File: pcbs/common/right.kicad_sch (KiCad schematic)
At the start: 89 parts, among them J2 TRS

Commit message: first pass at the gecko
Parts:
- removed rEXLED? (x2): YS-SK6812MINI-E, kbd_local:YS-SK6812MINI-E, symbol kbd_local:YS-SK6812MINI-E
- removed rEXSW? (x2): RotaryEncoder_Switch, kbd_local:keyswitch_cherrymx_hotswap_1u_rotary_encoder_ec12, symbol Device:RotaryEncoder_Switch
- added rEXLED1, rEXLED2: YS-SK6812MINI-E, kbd_local:YS-SK6812MINI-E, symbol kbd_local:YS-SK6812MINI-E
- added rRE1, rRE2: RotaryEncoder, kbd:rotary_encoder_EC05E_Vert, symbol Device:RotaryEncoder
- added rRE1-2, rRE1-3, rRE2-2, rRE2-3: RotaryEncoder, kbd:rotary_encoder_EC05E, symbol Device:RotaryEncoder
- added rSW22, rSW23: SW_Push, kbd:keyswitch_cherrymx_hotswap_1u, symbol Switch:SW_Push
- rSW? (x4): footprint kbd:keyswitch_cherrymx_hotswap_1u -> kbd:keyswitch_choc12_hotswap_1u
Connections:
- net GNDR: now also rEXLED1.3 (VSS), rEXLED2.3 (VSS), rRE1-2.C, rRE1-3.C, rRE1.C, rRE2-2.C, rRE2-3.C, rRE2.C, rSW22.2, rSW23.2
- net RE0A: now also rRE1-2.A, rRE1-3.A, rRE1.A
- net RE1A: now also rRE2-2.A, rRE2-3.A, rRE2.A
- net REB: now also rRE1-2.B, rRE1-3.B, rRE1.B, rRE2-2.B, rRE2-3.B, rRE2.B
- net at rD?.1 (K), rLED?.1 (VDD), rLED?.1 (VDD)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: now also rEXLED1.1 (VDD), rEXLED2.1 (VDD)
- net at rLED?.4 (DIN): now also rEXLED1.2 (DOUT); no longer rLED?.2 (DOUT)
- net KEYEX1 renamed KEY22
- net KEY22: now also rSW22.1
- net KEYEX2 renamed KEY23
- net KEY23: now also rSW23.1
- new net: rEXLED1.4 (DIN), rEXLED2.2 (DOUT)
- new net: rEXLED2.4 (DIN), rLED?.2 (DOUT)

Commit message: moved subsheets across
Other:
- company: foostan -> Dane Evans
- title: Corne Right -> Gecko Right
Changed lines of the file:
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@@
 	(paper "A3")
 	(title_block
-		(title "Corne Right")
+		(title "Gecko Right")
 		(date "2023-10-07")
-		(rev "4.0.0")
-		(company "foostan")
+		(rev "1.0.0")
+		(company "Dane Evans")
+		(comment 1 "original: foostan's crkbd 4.1")
 	)
 	(junction
@@
 		)
 		(instances
-			(project "corne-chocolate"
+			(project "Gecko_choc"
 				(path "/4cc5d416-57f5-4147-8183-e03ae6b1198a/50d96a5e-3d25-4129-9495-15388c76587f"
 					(reference "#PWR085")
@@
 		)
 		(instances
-			(project "corne-chocolate"
+			(project "Gecko_choc"
 				(path "/4cc5d416-57f5-4147-8183-e03ae6b1198a/50d96a5e-3d25-4129-9495-15388c76587f"
 					(reference "#PWR087")
@@
 				)
 			)
-			(project "corne-cherry"
+			(project "Gecko_choc"
 				(path "/4cc5d416-57f5-4147-8183-e03ae6b1198a/50d96a5e-3d25-4129-9495-15388c76587f"
 					(reference "#PWR070")
@@
 				)
 			)
-			(project "corne-cherry"
+			(project "Gecko_choc"
 				(path "/4cc5d416-57f5-4147-8183-e03ae6b1198a/50d96a5e-3d25-4129-9495-15388c76587f"
 					(reference "#PWR065")
@@
 				)
 			)
-			(project "corne-cherry"
+			(project "Gecko_choc"
 				(path "/4cc5d416-57f5-4147-8183-e03ae6b1198a/50d96a5e-3d25-4129-9495-15388c76587f"
 					(reference "#PWR069")
@@
 				)
 			)
-			(project "corne-cherry"
+			(project "Gecko_choc"
 				(path "/4cc5d416-57f5-4147-8183-e03ae6b1198a/50d96a5e-3d25-4129-9495-15388c76587f"
 					(reference "rBT4")
@@
 		)
 		(instances
-			(project "corne-chocolate"
+			(project "Gecko_choc"
 				(path "/4cc5d416-57f5-4147-8183-e03ae6b1198a/50d96a5e-3d25-4129-9495-15388c76587f"
 					(reference "rEXLED1")
@@
 				)
 			)
-			(project "corne-cherry"
+			(project "Gecko_choc"
 				(path "/4cc5d416-57f5-4147-8183-e03ae6b1198a/50d96a5e-3d25-4129-9495-15388c76587f"
 					(reference "#PWR066")
@@
 		)
 		(instances
-			(project "corne-chocolate"
+			(project "Gecko_choc"
 				(path "/4cc5d416-57f5-4147-8183-e03ae6b1198a/50d96a5e-3d25-4129-9495-15388c76587f"
 					(reference "rRE2")
@@
 		)
 		(instances
-			(project "corne-chocolate"
+			(project "Gecko_choc"
 				(path "/4cc5d416-57f5-4147-8183-e03ae6b1198a/50d96a5e-3d25-4129-9495-15388c76587f"
 					(reference "rRE1")
@@
 		)
 		(instances
-			(project "corne-chocolate"
+			(project "Gecko_choc"
 				(path "/4cc5d416-57f5-4147-8183-e03ae6b1198a/50d96a5e-3d25-4129-9495-15388c76587f"
 					(reference "#PWR059")
@@
 		)
 		(instances
-			(project "corne-chocolate"
+			(project "Gecko_choc"
 				(path "/4cc5d416-57f5-4147-8183-e03ae6b1198a/50d96a5e-3d25-4129-9495-15388c76587f"
 					(reference "rRE1-2")
@@
 				)
 			)
-			(project "corne-cherry"
+			(project "Gecko_choc"
 				(path "/4cc5d416-57f5-4147-8183-e03ae6b1198a/50d96a5e-3d25-4129-9495-15388c76587f"
 					(reference "#PWR073")
@@
 				)
 			)
-			(project "corne-cherry"
+			(project "Gecko_choc"
 				(path "/4cc5d416-57f5-4147-8183-e03ae6b1198a/50d96a5e-3d25-4129-9495-15388c76587f"
 					(reference "#PWR068")
@@
 		)
 		(instances
-			(project "corne-chocolate"
+			(project "Gecko_choc"
 				(path "/4cc5d416-57f5-4147-8183-e03ae6b1198a/50d96a5e-3d25-4129-9495-15388c76587f"
 					(reference "rSW22")
@@
 		)
 		(instances
-			(project "corne-chocolate"
+			(project "Gecko_choc"
 				(path "/4cc5d416-57f5-4147-8183-e03ae6b1198a/50d96a5e-3d25-4129-9495-15388c76587f"
 					(reference "rRE2-3")
@@
 		)
 		(instances
-			(project "corne-chocolate"
+			(project "Gecko_choc"
 				(path "/4cc5d416-57f5-4147-8183-e03ae6b1198a/50d96a5e-3d25-4129-9495-15388c76587f"
 					(reference "rRE2-2")
@@
 				)
 			)
-			(project "corne-cherry"
+			(project "Gecko_choc"
 				(path "/4cc5d416-57f5-4147-8183-e03ae6b1198a/50d96a5e-3d25-4129-9495-15388c76587f"
 					(reference "#PWR07")
@@
 		)
 		(instances
-			(project "corne-chocolate"
+			(project "Gecko_choc"
 				(path "/4cc5d416-57f5-4147-8183-e03ae6b1198a/50d96a5e-3d25-4129-9495-15388c76587f"
 					(reference "#PWR084")
@@
 				)
 			)
-			(project "corne-cherry"
+			(project "Gecko_choc"
 				(path "/4cc5d416-57f5-4147-8183-e03ae6b1198a/50d96a5e-3d25-4129-9495-15388c76587f"
 					(reference "#PWR075")
@@
 		)
 		(instances
-			(project "corne-chocolate"
+			(project "Gecko_choc"
 				(path "/4cc5d416-57f5-4147-8183-e03ae6b1198a/50d96a5e-3d25-4129-9495-15388c76587f"
 					(reference "#PWR086")
@@
 				)
 			)
-			(project "corne-cherry"
+			(project "Gecko_choc"
 				(path "/4cc5d416-57f5-4147-8183-e03ae6b1198a/50d96a5e-3d25-4129-9495-15388c76587f"
 					(reference "#PWR072")
@@
 		)
 		(instances
-			(project "corne-chocolate"
+			(project "Gecko_choc"
 				(path "/4cc5d416-57f5-4147-8183-e03ae6b1198a/50d96a5e-3d25-4129-9495-15388c76587f"
 					(reference "rEXLED2")
@@
 				)
 			)
-			(project "corne-cherry"
+			(project "Gecko_choc"
 				(path "/4cc5d416-57f5-4147-8183-e03ae6b1198a/50d96a5e-3d25-4129-9495-15388c76587f"
 					(reference "#PWR067")
@@
 				)
 			)
-			(project "corne-cherry"
+			(project "Gecko_choc"
 				(path "/4cc5d416-57f5-4147-8183-e03ae6b1198a/50d96a5e-3d25-4129-9495-15388c76587f"
 					(reference "#PWR071")
@@
 		)
 		(instances
-			(project "corne-chocolate"
+			(project "Gecko_choc"
 				(path "/4cc5d416-57f5-4147-8183-e03ae6b1198a/50d96a5e-3d25-4129-9495-15388c76587f"
 					(reference "#PWR074")
@@
 		)
 		(instances
-			(project "corne-chocolate"
+			(project "Gecko_choc"
 				(path "/4cc5d416-57f5-4147-8183-e03ae6b1198a/50d96a5e-3d25-4129-9495-15388c76587f"
 					(reference "rRE1-3")
@@
 				)
 			)
-			(project "corne-cherry"
+			(project "Gecko_choc"
 				(path "/4cc5d416-57f5-4147-8183-e03ae6b1198a/50d96a5e-3d25-4129-9495-15388c76587f"
 					(reference "rBT3")
@@
 		)
 		(instances
-			(project "corne-chocolate"
+			(project "Gecko_choc"
 				(path "/4cc5d416-57f5-4147-8183-e03ae6b1198a/50d96a5e-3d25-4129-9495-15388c76587f"
 					(reference "rSW23")
@@
 				)
 			)
-			(project "corne-cherry"
+			(project "Gecko_choc"
 				(path "/4cc5d416-57f5-4147-8183-e03ae6b1198a/50d96a5e-3d25-4129-9495-15388c76587f"
 					(reference "rJP1")
@@
 				)
 			)
-			(project "corne-cherry"
+			(project "Gecko_choc"
 				(path "/4cc5d416-57f5-4147-8183-e03ae6b1198a/50d96a5e-3d25-4129-9495-15388c76587f"
 					(reference "rBT1")
@@
 				)
 			)
-			(project "corne-cherry"
+			(project "Gecko_choc"
 				(path "/4cc5d416-57f5-4147-8183-e03ae6b1198a/50d96a5e-3d25-4129-9495-15388c76587f"
 					(reference "#PWR076")
@@
 				)
 			)
-			(project "corne-cherry"
+			(project "Gecko_choc"
 				(path "/4cc5d416-57f5-4147-8183-e03ae6b1198a/50d96a5e-3d25-4129-9495-15388c76587f"
 					(reference "rBT2")

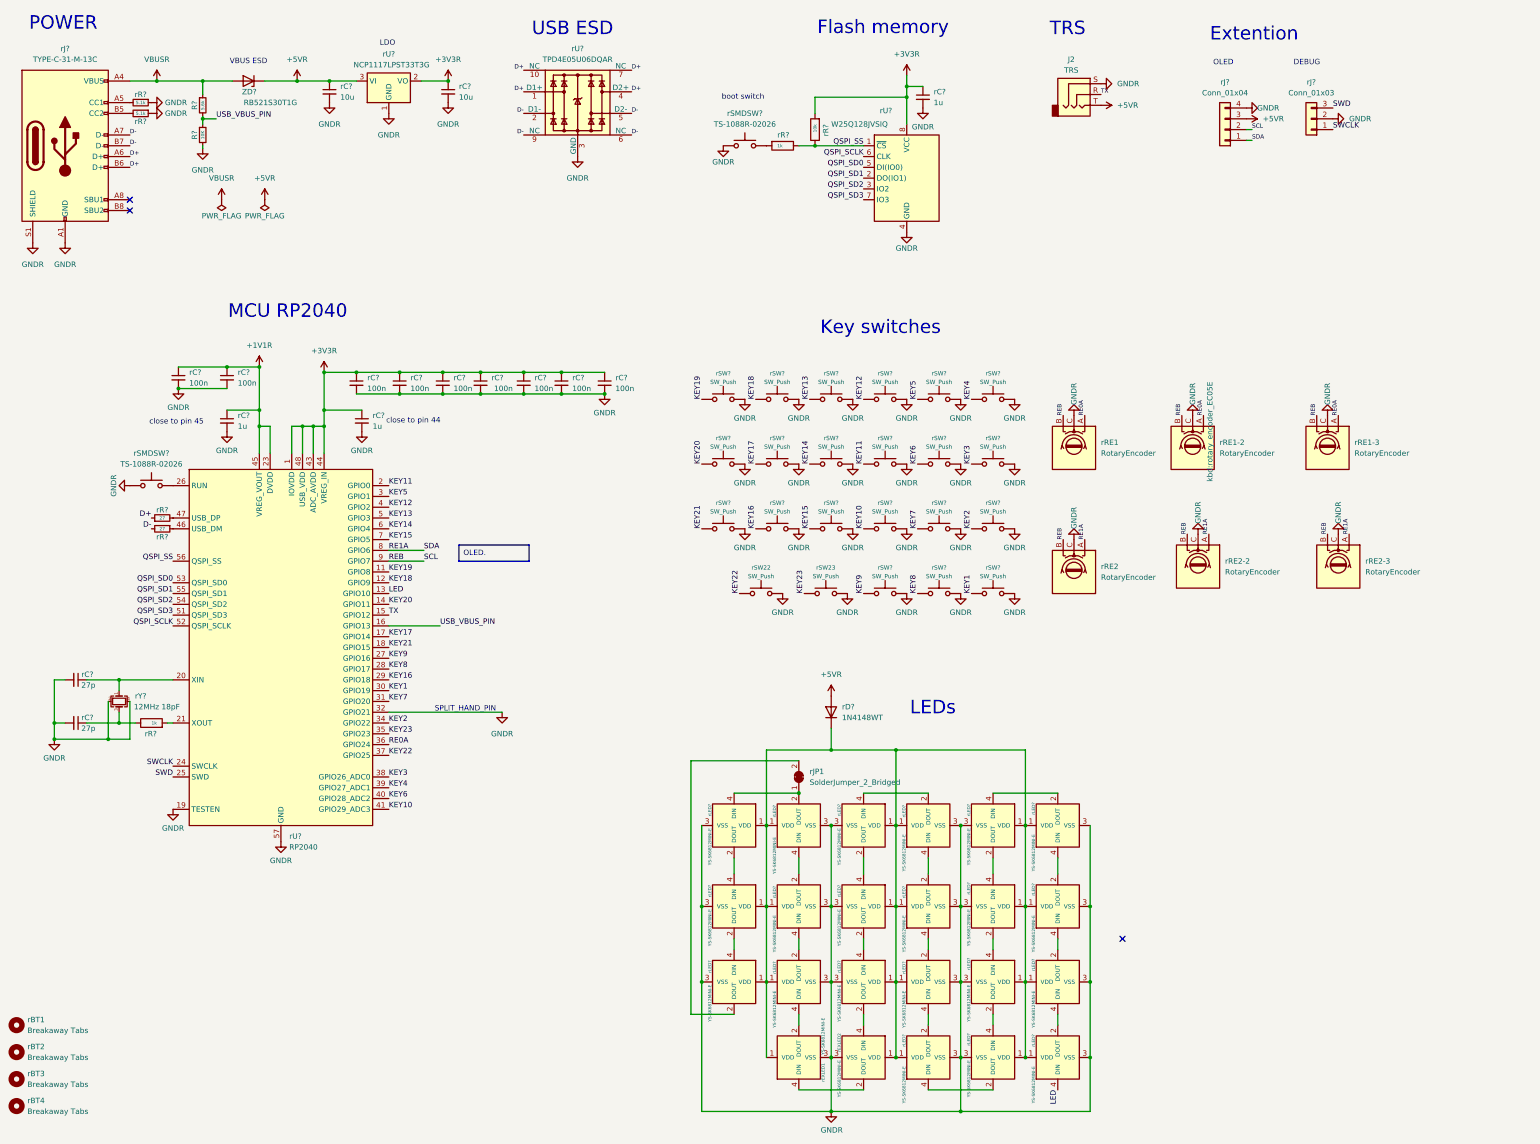
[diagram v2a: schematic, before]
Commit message: add jumpers to the split pin
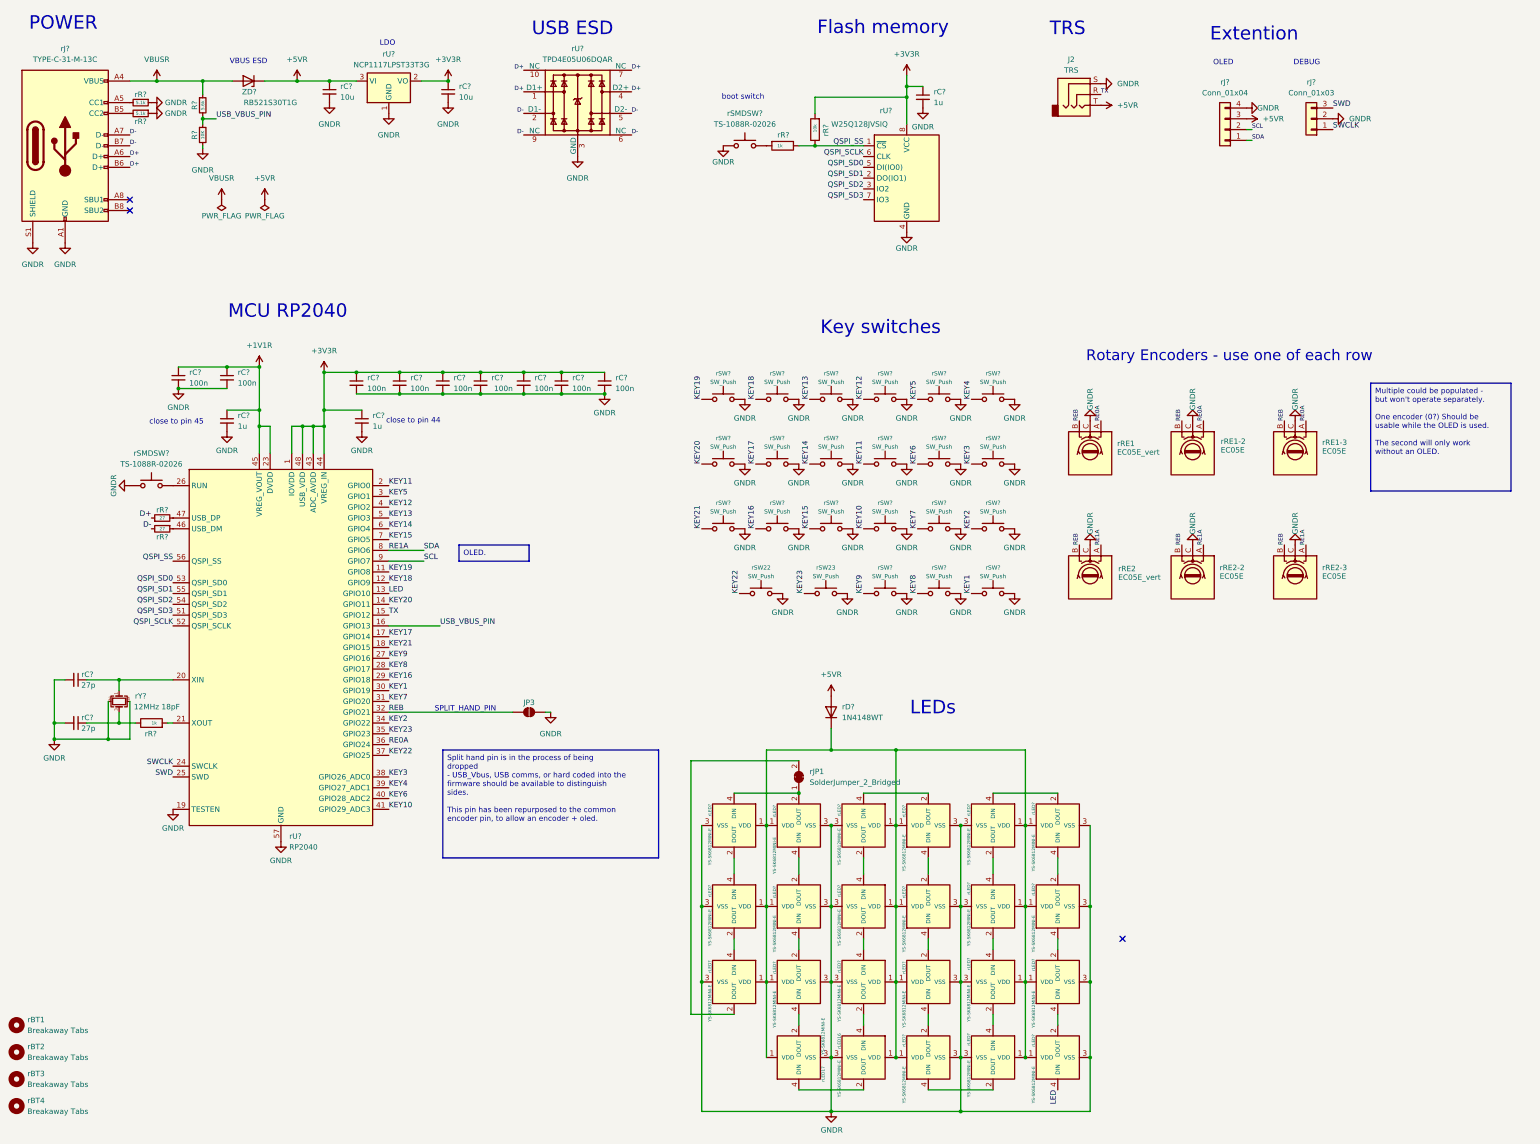
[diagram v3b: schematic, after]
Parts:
- added JP3: SolderJumper_2_Open, Jumper:SolderJumper-2_P1.3mm_Open_RoundedPad1.0x1.5mm, symbol Jumper:SolderJumper_2_Open
- rLED16: renamed from rEXLED2; footprint kbd_local:YS-SK6812MINI-E -> kbd:YS-SK6812MINI-E
- rLED17: renamed from rEXLED1; footprint kbd_local:YS-SK6812MINI-E -> kbd:YS-SK6812MINI-E
- rLED? (x21): footprint kbd_local:YS-SK6812MINI-E -> kbd:YS-SK6812MINI-E
- rRE1, rRE2: value RotaryEncoder -> EC05E_vert
- rRE1-2, rRE1-3, rRE2-2, rRE2-3: value RotaryEncoder -> EC05E
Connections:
- net GNDR: now also JP3.2 (B); no longer rU?.32 (GPIO21)
- net REB: now also rU?.32 (GPIO21), JP3.1 (A); no longer rJ?.2 (Pin_2), rU?.9 (GPIO7)
- new net SCL: rJ?.2 (Pin_2), rU?.9 (GPIO7)
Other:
- note added: "Rotary Encoders - use one of each row"
- moved on the sheet: rRE1, rRE1-2, rRE1-3, rRE2, rRE2-2, rRE2-3

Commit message: allDRC
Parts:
- J2: footprint kbd_local:PJ-398A-5A_PJ-399B-6A -> kbd:PJ-398A-5A_PJ-399B-6A
- rBT1, rBT2, rBT3, rBT4: footprint kbd_local:Breakaway_Tabs -> kbd:Breakaway_Tabs
- rJ?: footprint kbd_local:TYPE-C-31-M-13C -> kbd:TYPE-C-31-M-13C
- rJ?: footprint kbd_local:OLED -> kbd:OLED
- rSMDSW? (x2): footprint kbd_local:TS-1088R-02026 -> kbd:TS-1088R-02026
- rSW22, rSW23, rSW? (x16): footprint kbd:keyswitch_cherrymx_hotswap_1u -> kbd:keyswitch_choc12_hotswap_1u
- rSW?: footprint kbd:keyswitch_cherrymx_hotswap_1.5u -> kbd:keyswitch_choc12_hotswap_1.5u
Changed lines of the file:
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@@
 			)
 		)
-		(property "Footprint" "kbd:keyswitch_cherrymx_hotswap_1u"
+		(property "Footprint" "kbd:keyswitch_choc12_hotswap_1u"
 			(at 236.22 118.11 0)
 			(effects
@@
 			)
 		)
-		(property "Footprint" "kbd:keyswitch_cherrymx_hotswap_1u"
+		(property "Footprint" "kbd:keyswitch_choc12_hotswap_1u"
 			(at 248.92 102.87 0)
 			(effects
@@
 			)
 		)
-		(property "Footprint" "kbd_local:TYPE-C-31-M-13C"
+		(property "Footprint" "kbd:TYPE-C-31-M-13C"
 			(at 34.29 48.26 0)
 			(effects
@@
 			)
 		)
-		(property "Footprint" "kbd:keyswitch_cherrymx_hotswap_1u"
+		(property "Footprint" "kbd:keyswitch_choc12_hotswap_1u"
 			(at 236.22 102.87 0)
 			(effects
@@
 			)
 		)
-		(property "Footprint" "kbd:keyswitch_cherrymx_hotswap_1u"
+		(property "Footprint" "kbd:keyswitch_choc12_hotswap_1u"
 			(at 198.12 133.35 0)
 			(effects
@@
 			)
 		)
-		(property "Footprint" "kbd:keyswitch_cherrymx_hotswap_1u"
+		(property "Footprint" "kbd:keyswitch_choc12_hotswap_1u"
 			(at 210.82 133.35 0)
 			(effects
@@
 			)
 		)
-		(property "Footprint" "kbd:keyswitch_cherrymx_hotswap_1.5u"
+		(property "Footprint" "kbd:keyswitch_choc12_hotswap_1.5u"
 			(at 248.92 148.59 0)
 			(effects
@@
 			)
 		)
-		(property "Footprint" "kbd_local:Breakaway_Tabs"
+		(property "Footprint" "kbd:Breakaway_Tabs"
 			(at 19.05 274.32 0)
 			(effects
@@
 			)
 		)
-		(property "Footprint" "kbd:keyswitch_cherrymx_hotswap_1u"
+		(property "Footprint" "kbd:keyswitch_choc12_hotswap_1u"
 			(at 198.12 118.11 0)
 			(effects
@@
 			)
 		)
-		(property "Footprint" "kbd:keyswitch_cherrymx_hotswap_1u"
+		(property "Footprint" "kbd:keyswitch_choc12_hotswap_1u"
 			(at 185.42 133.35 0)
 			(effects
@@
 			)
 		)
-		(property "Footprint" "kbd:keyswitch_cherrymx_hotswap_1u"
+		(property "Footprint" "kbd:keyswitch_choc12_hotswap_1u"
 			(at 194.31 148.59 0)
 			(effects
@@
 			)
 		)
-		(property "Footprint" "kbd:keyswitch_cherrymx_hotswap_1u"
+		(property "Footprint" "kbd:keyswitch_choc12_hotswap_1u"
 			(at 223.52 148.59 0)
 			(effects
@@
 			)
 		)
-		(property "Footprint" "kbd_local:PJ-398A-5A_PJ-399B-6A"
+		(property "Footprint" "kbd:PJ-398A-5A_PJ-399B-6A"
 			(at 269.24 36.195 0)
 			(effects
@@
 			)
 		)
-		(property "Footprint" "kbd:keyswitch_cherrymx_hotswap_1u"
+		(property "Footprint" "kbd:keyswitch_choc12_hotswap_1u"
 			(at 248.92 133.35 0)
 			(effects
@@
 			)
 		)
-		(property "Footprint" "kbd:keyswitch_cherrymx_hotswap_1u"
+		(property "Footprint" "kbd:keyswitch_choc12_hotswap_1u"
 			(at 236.22 133.35 0)
 			(effects
@@
 			)
 		)
-		(property "Footprint" "kbd_local:TS-1088R-02026"
+		(property "Footprint" "kbd:TS-1088R-02026"
 			(at 50.8 123.19 0)
 			(effects
@@
 			)
 		)
-		(property "Footprint" "kbd:keyswitch_cherrymx_hotswap_1u"
+		(property "Footprint" "kbd:keyswitch_choc12_hotswap_1u"
 			(at 210.82 118.11 0)
 			(effects
@@
 			)
 		)
-		(property "Footprint" "kbd:keyswitch_cherrymx_hotswap_1u"
+		(property "Footprint" "kbd:keyswitch_choc12_hotswap_1u"
 			(at 248.92 118.11 0)
 			(effects
@@
 			)
 		)
-		(property "Footprint" "kbd:keyswitch_cherrymx_hotswap_1u"
+		(property "Footprint" "kbd:keyswitch_choc12_hotswap_1u"
 			(at 185.42 118.11 0)
 			(effects
@@
 			)
 		)
-		(property "Footprint" "kbd_local:OLED"
+		(property "Footprint" "kbd:OLED"
 			(at 303.53 44.45 0)
 			(effects
@@
 			)
 		)
-		(property "Footprint" "kbd:keyswitch_cherrymx_hotswap_1u"
+		(property "Footprint" "kbd:keyswitch_choc12_hotswap_1u"
 			(at 223.52 118.11 0)
 			(effects
@@
 			)
 		)
-		(property "Footprint" "kbd_local:TS-1088R-02026"
+		(property "Footprint" "kbd:TS-1088R-02026"
 			(at 190.5 43.18 0)
 			(effects
@@
 			)
 		)
-		(property "Footprint" "kbd_local:Breakaway_Tabs"
+		(property "Footprint" "kbd:Breakaway_Tabs"
 			(at 19.05 267.97 0)
 			(effects
@@
 			)
 		)
-		(property "Footprint" "kbd:keyswitch_cherrymx_hotswap_1u"
+		(property "Footprint" "kbd:keyswitch_choc12_hotswap_1u"
 			(at 236.22 148.59 0)
 			(effects
@@
 			)
 		)
-		(property "Footprint" "kbd:keyswitch_cherrymx_hotswap_1u"
+		(property "Footprint" "kbd:keyswitch_choc12_hotswap_1u"
 			(at 209.55 148.59 0)
 			(effects
@@
 			)
 		)
-		(property "Footprint" "kbd:keyswitch_cherrymx_hotswap_1u"
+		(property "Footprint" "kbd:keyswitch_choc12_hotswap_1u"
 			(at 223.52 133.35 0)
 			(effects
@@
 			)
 		)
-		(property "Footprint" "kbd_local:Breakaway_Tabs"
+		(property "Footprint" "kbd:Breakaway_Tabs"
 			(at 19.05 255.27 0)
 			(effects
@@
 			)
 		)
-		(property "Footprint" "kbd_local:Breakaway_Tabs"
+		(property "Footprint" "kbd:Breakaway_Tabs"
 			(at 19.05 261.62 0)
 			(effects
